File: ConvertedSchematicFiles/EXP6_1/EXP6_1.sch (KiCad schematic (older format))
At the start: 8 parts

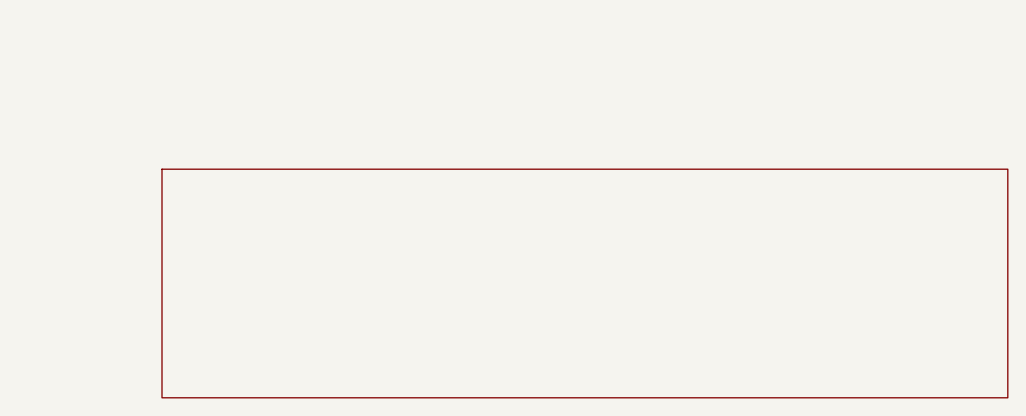
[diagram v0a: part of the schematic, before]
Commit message: Excluded some components. These no longer appear after conversion. When calling shell commands, filenames are in "quotes"
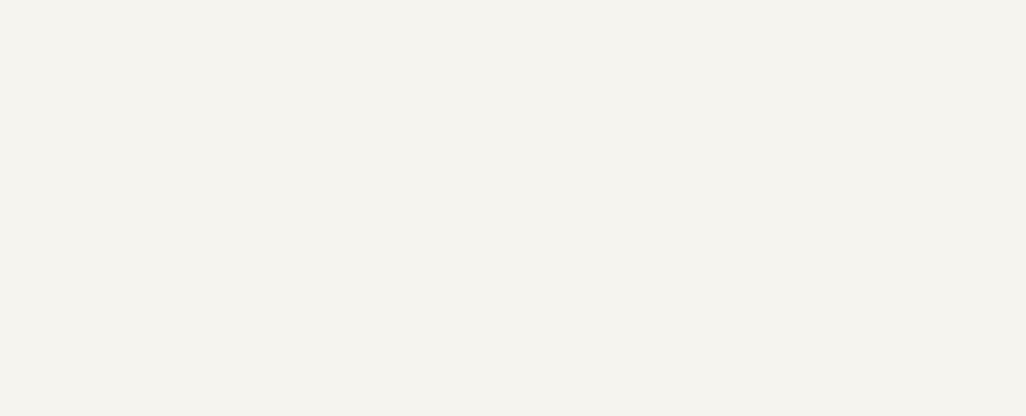
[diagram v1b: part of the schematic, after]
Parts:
- removed titleblk: titleblk, symbol TITLEBLK_PSPICE
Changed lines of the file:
@@
-	1    0    0    1
-$EndComp
-$Comp
-L TITLEBLK_PSPICE titleblk
-U 1 1 39760492
-P 9700 7200
-F 0 "titleblk" H 19400 14400 30  0001 L CNN
-F 1 "titleblk" H 19400 14480 30  0001 L CNN
-	1    9700 7200
 	1    0    0    1
 $EndComp

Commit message: Ports issue fixed. Now annotation for ports is #PWR? function added "itos"
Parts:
- removed EGND: EGND, symbol EGND_PSPICE
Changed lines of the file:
@@
 $EndDescr
 $Comp
-L EGND_PSPICE EGND
+L EGND_PSPICE #PWR1
 U 1 1 14289383
 P 3000 1600
-F 0 "EGND" H 6000 3200 30  0001 L CNN
+F 0 "#PWR1" H 6000 3200 30  0001 L CNN
 F 1 "EGND" H 6000 3280 30  0001 L CNN
 	1    3000 1600

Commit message: Added LICENSE.txt
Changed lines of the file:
@@
 $EndDescr
 $Comp
-L EGND_PSPICE #PWR1
+L GND #PWR1
 U 1 1 14289383
 P 3000 1600

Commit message: Orientation fix. Library components are now inverted, with +ve y axis going up. In Schematic files, +ve y axis is downwards. This is how the KiCad libraries are. As a result of the above fixed, the converted GND is now oriented correctly.
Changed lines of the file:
@@
 F 1 "EGND" H 6000 3280 30  0001 L CNN
 	1    3000 1600
-	1    0    0    1
+	1    0    0    -1
 $EndComp
 $Comp
@@
 F 1 "2K" H 1800 1150 30  0000 L CNN
 	1    1800 1000
-	1    0    0    1
+	1    0    0    -1
 $EndComp
 $Comp
@@
 F 1 "3k" H 2400 1150 30  0000 L CNN
 	1    2400 1000
-	1    0    0    1
+	1    0    0    -1
 $EndComp
 $Comp
@@
 F 1 "6V" H 3000 1090 30  0000 C CNN
 	1    3000 1200
-	1    0    0    1
+	1    0    0    -1
 $EndComp
 $Comp
@@
 F 1 "12V" H 1000 1090 30  0000 C CNN
 	1    1000 1200
-	1    0    0    1
+	1    0    0    -1
 $EndComp
 $Comp
@@
 F 1 "INCLUDE" H 1300 1980 30  0001 L CNN
 	1    1300 1900
-	1    0    0    1
+	1    0    0    -1
 $EndComp
 $Comp
@@
 F 1 "1k" H 1200 1150 30  0000 L CNN
 	1    1200 1000
-	1    0    0    1
+	1    0    0    -1
 $EndComp
 Wire Wire Line

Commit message: Removed the use of exec, wrote basename function, made integration with eSim easier.
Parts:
- added titleblk: titleblk, symbol titleblk_PSPICE
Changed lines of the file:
@@
-EESchema Schematic File Version 2  date Friday 25 February 2000 06:54:54 PM IST
+EESchema Schematic File Version 2  date
 LIBS:power
 LIBS:device
@@
 LIBS:contrib
 LIBS:valves
-LIBS:ConvertedSchematicFiles/EXP6_1-cache
 EELAYER 25  0
 EELAYER END
@@
 Sheet 1 1
 Title ""
-Date "25 Feb 2000"
+Date ""
 Rev ""
 Comp ""
@@
 	1    0    0    -1
 $EndComp
+$Comp
+L titleblk_PSPICE titleblk
+U 1 1 39760492
+P 9700 7200
+F 0 "titleblk" H 19400 14400 30  0001 L CNN
+F 1 "titleblk" H 19400 14480 30  0001 L CNN
+	1    9700 7200
+	1    0    0    -1
+$EndComp
